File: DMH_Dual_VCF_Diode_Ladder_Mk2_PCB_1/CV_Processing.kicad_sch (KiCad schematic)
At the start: 46 parts, among them J15 Conn_01x08_PinHeader, J16 Conn_01x08_PinHeader, SW10 SW_DPDT_OnOn, SW7 SW_SPDT_OnOffOn, SW9 SW_SPDT_OnOffOn, U7 TL074, U8 TL074

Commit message: Corrected pin header footprint assignments
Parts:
- J15, J16: footprint Connector_PinHeader_2.54mm:PinHeader_1x10_P2.54mm_Vertical -> Connector_PinHeader_2.54mm:PinHeader_1x08_P2.54mm_Vertical
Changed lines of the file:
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@@
 			)
 		)
-		(property "Footprint" "Connector_PinHeader_2.54mm:PinHeader_1x10_P2.54mm_Vertical"
+		(property "Footprint" "Connector_PinHeader_2.54mm:PinHeader_1x08_P2.54mm_Vertical"
 			(at 69.85 106.68 0)
 			(effects
@@
 			)
 		)
-		(property "Footprint" "Connector_PinHeader_2.54mm:PinHeader_1x10_P2.54mm_Vertical"
+		(property "Footprint" "Connector_PinHeader_2.54mm:PinHeader_1x08_P2.54mm_Vertical"
 			(at 63.5 81.28 0)
 			(effects
@@
 			)
 		)
-		(property "Footprint" "Connector_PinHeader_2.54mm:PinHeader_1x10_P2.54mm_Vertical"
+		(property "Footprint" "Connector_PinHeader_2.54mm:PinHeader_1x08_P2.54mm_Vertical"
 			(at 119.38 38.1 0)
 			(effects
@@
 			)
 		)
-		(property "Footprint" "Connector_PinHeader_2.54mm:PinHeader_1x10_P2.54mm_Vertical"
+		(property "Footprint" "Connector_PinHeader_2.54mm:PinHeader_1x08_P2.54mm_Vertical"
 			(at 160.02 101.6 0)
 			(effects
@@
 			)
 		)
-		(property "Footprint" "Connector_PinHeader_2.54mm:PinHeader_1x10_P2.54mm_Vertical"
+		(property "Footprint" "Connector_PinHeader_2.54mm:PinHeader_1x08_P2.54mm_Vertical"
 			(at 140.97 101.6 0)
 			(effects
@@
 			)
 		)
-		(property "Footprint" "Connector_PinHeader_2.54mm:PinHeader_1x10_P2.54mm_Vertical"
+		(property "Footprint" "Connector_PinHeader_2.54mm:PinHeader_1x08_P2.54mm_Vertical"
 			(at 52.07 201.93 0)
 			(effects
@@
 			)
 		)
-		(property "Footprint" "Connector_PinHeader_2.54mm:PinHeader_1x10_P2.54mm_Vertical"
+		(property "Footprint" "Connector_PinHeader_2.54mm:PinHeader_1x08_P2.54mm_Vertical"
 			(at 127 170.18 0)
 			(effects
@@
 			)
 		)
-		(property "Footprint" "Connector_PinHeader_2.54mm:PinHeader_1x10_P2.54mm_Vertical"
+		(property "Footprint" "Connector_PinHeader_2.54mm:PinHeader_1x08_P2.54mm_Vertical"
 			(at 38.1 182.88 0)
 			(effects
@@
 			)
 		)
-		(property "Footprint" "Connector_PinHeader_2.54mm:PinHeader_1x10_P2.54mm_Vertical"
+		(property "Footprint" "Connector_PinHeader_2.54mm:PinHeader_1x08_P2.54mm_Vertical"
 			(at 77.47 227.33 0)
 			(effects
@@
 			)
 		)
-		(property "Footprint" "Connector_PinHeader_2.54mm:PinHeader_1x10_P2.54mm_Vertical"
+		(property "Footprint" "Connector_PinHeader_2.54mm:PinHeader_1x08_P2.54mm_Vertical"
 			(at 77.47 100.33 0)
 			(effects
@@
 			)
 		)
-		(property "Footprint" "Connector_PinHeader_2.54mm:PinHeader_1x10_P2.54mm_Vertical"
+		(property "Footprint" "Connector_PinHeader_2.54mm:PinHeader_1x08_P2.54mm_Vertical"
 			(at 63.5 208.28 0)
 			(effects
@@
 			)
 		)
-		(property "Footprint" "Connector_PinHeader_2.54mm:PinHeader_1x10_P2.54mm_Vertical"
+		(property "Footprint" "Connector_PinHeader_2.54mm:PinHeader_1x08_P2.54mm_Vertical"
 			(at 140.97 177.8 0)
 			(effects
@@
 			)
 		)
-		(property "Footprint" "Connector_PinHeader_2.54mm:PinHeader_1x10_P2.54mm_Vertical"
+		(property "Footprint" "Connector_PinHeader_2.54mm:PinHeader_1x08_P2.54mm_Vertical"
 			(at 171.45 134.62 0)
 			(effects
@@
 			)
 		)
-		(property "Footprint" "Connector_PinHeader_2.54mm:PinHeader_1x10_P2.54mm_Vertical"
+		(property "Footprint" "Connector_PinHeader_2.54mm:PinHeader_1x08_P2.54mm_Vertical"
 			(at 38.1 55.88 0)
 			(effects
@@
 			)
 		)
-		(property "Footprint" "Connector_PinHeader_2.54mm:PinHeader_1x10_P2.54mm_Vertical"
+		(property "Footprint" "Connector_PinHeader_2.54mm:PinHeader_1x08_P2.54mm_Vertical"
 			(at 52.07 74.93 0)
 			(effects
@@
 			)
 		)
-		(property "Footprint" "Connector_PinHeader_2.54mm:PinHeader_1x10_P2.54mm_Vertical"
+		(property "Footprint" "Connector_PinHeader_2.54mm:PinHeader_1x08_P2.54mm_Vertical"
 			(at 69.85 233.68 0)
 			(effects

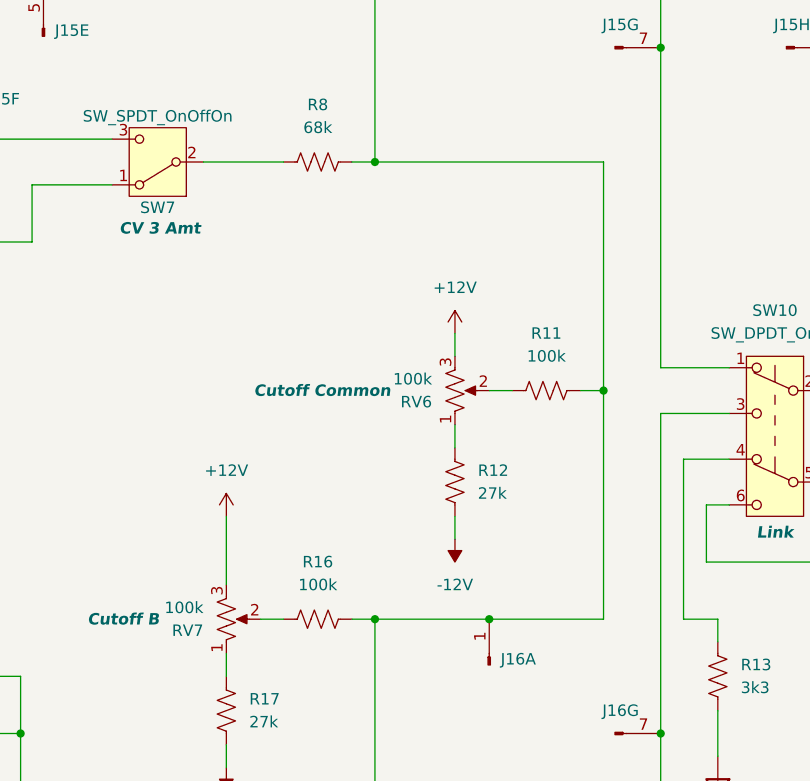
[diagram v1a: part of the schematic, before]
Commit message: Replaced Central Cutoff pot with dual port
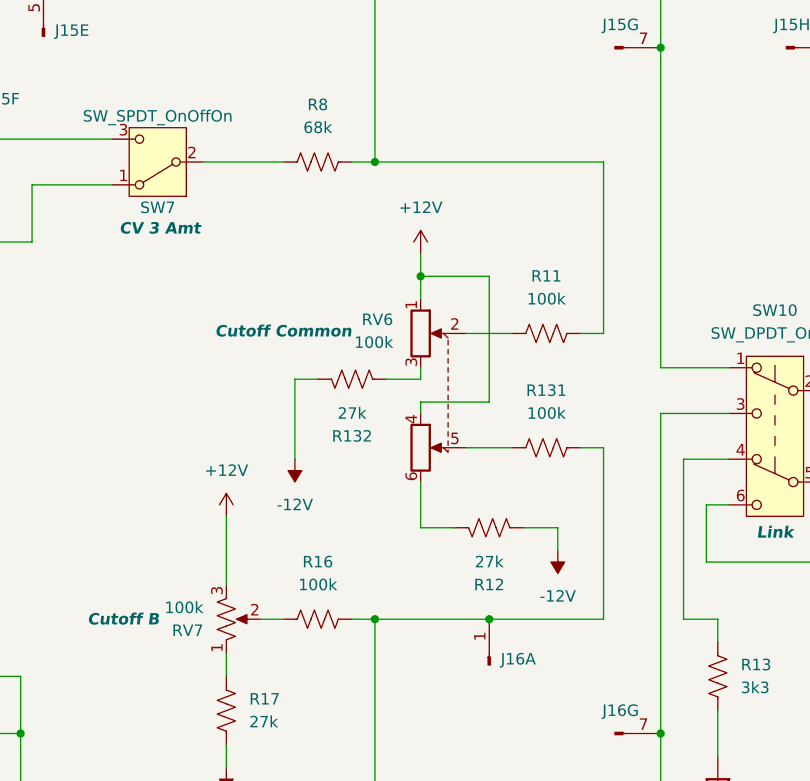
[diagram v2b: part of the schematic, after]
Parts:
- removed RV6: 100k, SynthStuff:Potentiometer_Alpha_RD901F-40-00D_Single_Vertical, symbol Device:R_Potentiometer_US
- added R131: 100k, Resistor_THT:R_Axial_DIN0207_L6.3mm_D2.5mm_P7.62mm_Horizontal, symbol Device:R_US
- added R132: 27k, Resistor_THT:R_Axial_DIN0207_L6.3mm_D2.5mm_P7.62mm_Horizontal, symbol Device:R_US
- added RV6: 100k, Potentiometer_THT:Potentiometer_Alpha_RD902F-40-00D_Dual_Vertical, symbol Device:R_Potentiometer_Dual
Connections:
- net +12V: now also RV6.1, RV6.4
- net -12V: now also R12.1, R132.2; no longer R12.2
- net at J15.1 (Pin_1), R1.2, R11.2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: no longer J16.1 (Pin_1), R16.2, R19.2, R20.1, R22.2, R23.1, U8.13 (-)
- net at R11.1: now also RV6.2
- new net: J16.1 (Pin_1), R131.2, R16.2, R19.2, R20.1, R22.2, R23.1, U8.13 (-)
- new net: R131.1, RV6.5
- new net: R12.2, RV6.6
- new net: R132.1, RV6.3
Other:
- moved on the sheet: R11, R12

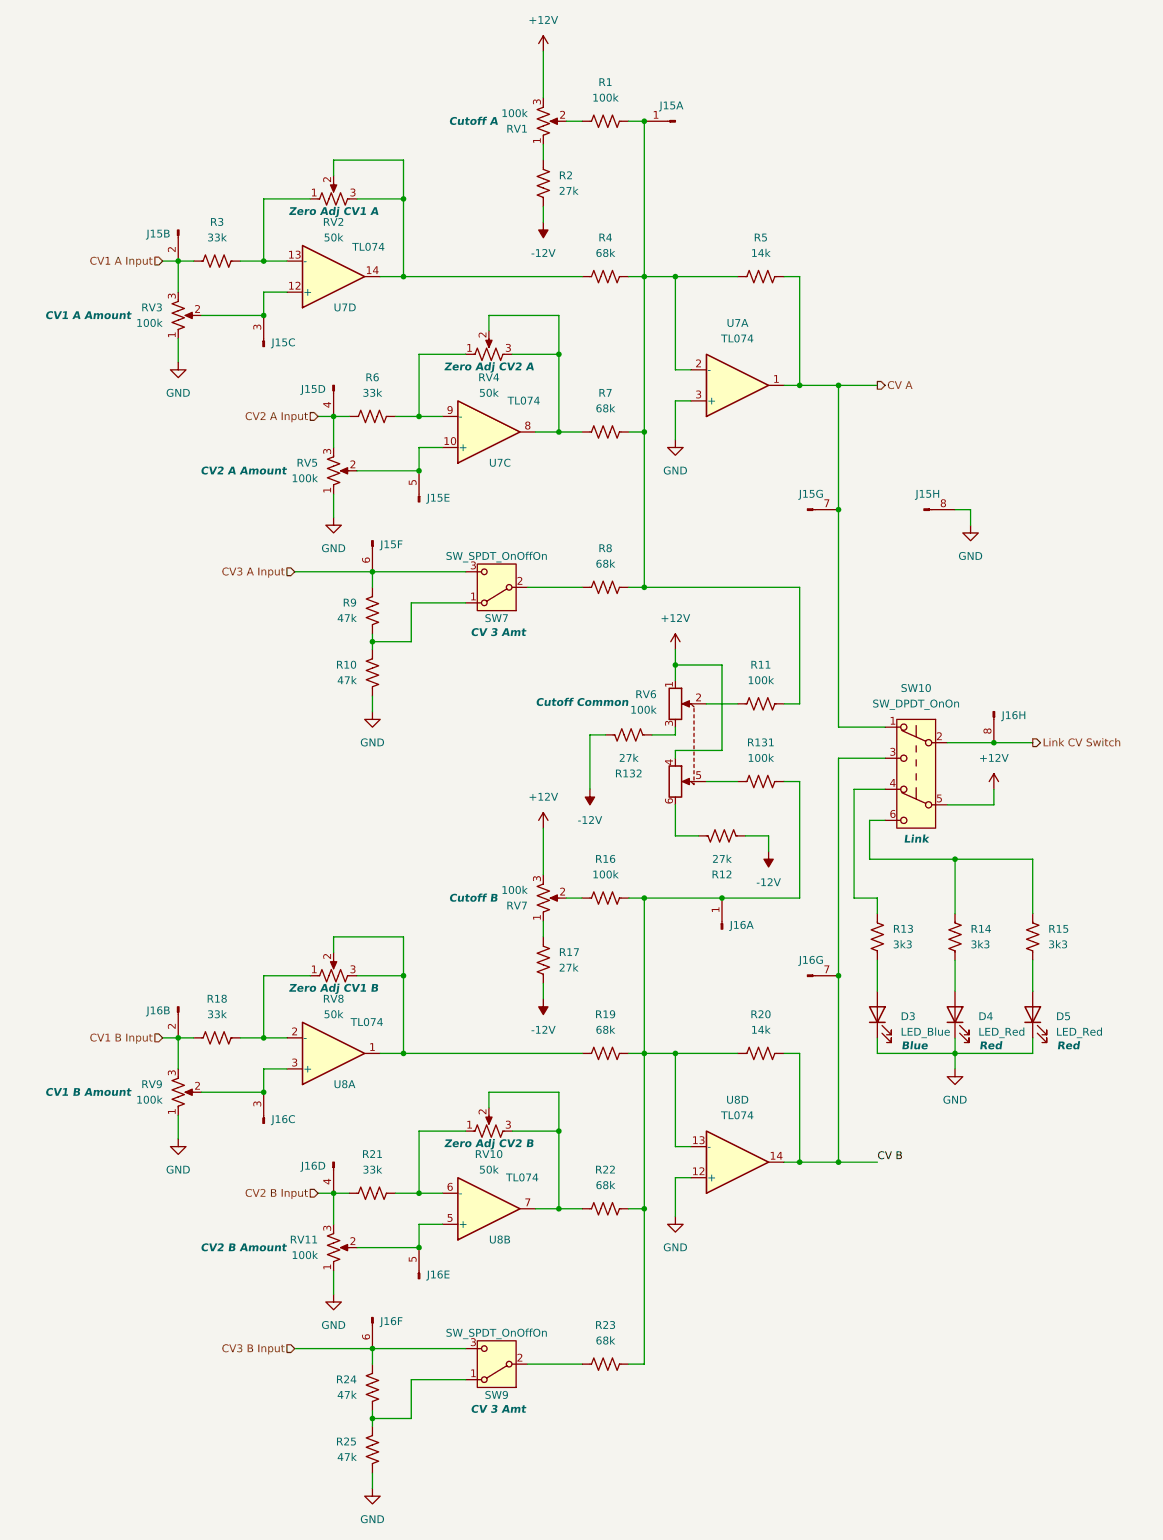
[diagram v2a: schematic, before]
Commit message: Routed circuit B
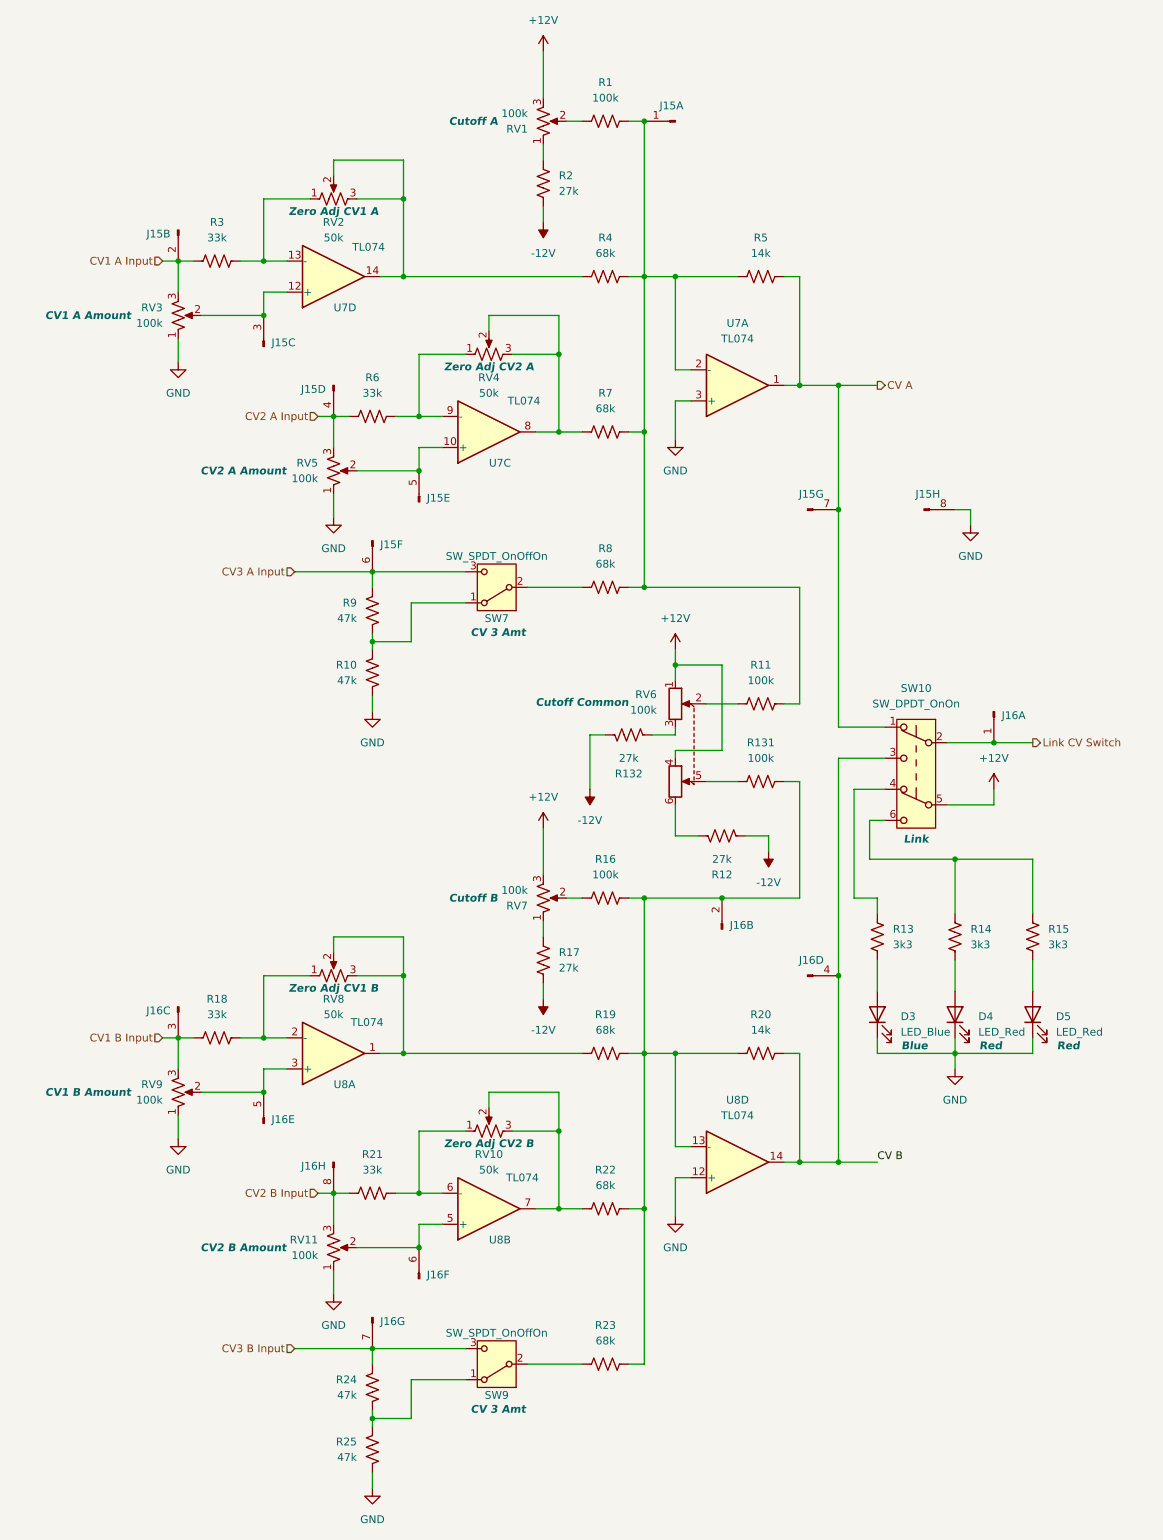
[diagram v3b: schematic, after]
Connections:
- net CV B: now also J16.4 (Pin_4); no longer J16.7 (Pin_7)
- net CV1 B Input: now also J16.3 (Pin_3); no longer J16.2 (Pin_2)
- net CV2 B Input: now also J16.8 (Pin_8); no longer J16.4 (Pin_4)
- net CV3 B Input: now also J16.7 (Pin_7); no longer J16.6 (Pin_6)
- net Link CV Switch: now also J16.1 (Pin_1); no longer J16.8 (Pin_8)
- net at R131.2, R16.2, R19.2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: now also J16.2 (Pin_2); no longer J16.1 (Pin_1)
- net at RV11.2, U8.5 (+): now also J16.6 (Pin_6); no longer J16.5 (Pin_5)
- net at RV9.2, U8.3 (+): now also J16.5 (Pin_5); no longer J16.3 (Pin_3)
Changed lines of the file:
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@@
 		(at 52.07 201.93 270)
 		(mirror x)
-		(unit 3)
+		(unit 5)
 		(exclude_from_sim no)
 		(in_bom yes)
@@
 				(path "/58f4306d-5387-4983-bb08-41a2313fd315/ec2d44bc-ed06-4f0b-a22e-df640fa5e089"
 					(reference "J16")
-					(unit 3)
+					(unit 5)
 				)
 			)
@@
 		(lib_id "SynthStuff:Conn_01x08_PinHeader")
 		(at 127 170.18 90)
-		(unit 1)
+		(unit 2)
 		(exclude_from_sim no)
 		(in_bom yes)
@@
 				(path "/58f4306d-5387-4983-bb08-41a2313fd315/ec2d44bc-ed06-4f0b-a22e-df640fa5e089"
 					(reference "J16")
-					(unit 1)
+					(unit 2)
 				)
 			)
@@
 		(at 38.1 182.88 90)
 		(mirror x)
-		(unit 2)
+		(unit 3)
 		(exclude_from_sim no)
 		(in_bom yes)
@@
 				(path "/58f4306d-5387-4983-bb08-41a2313fd315/ec2d44bc-ed06-4f0b-a22e-df640fa5e089"
 					(reference "J16")
-					(unit 2)
+					(unit 3)
 				)
 			)
@@
 		(lib_id "SynthStuff:Conn_01x08_PinHeader")
 		(at 77.47 227.33 90)
-		(unit 5)
+		(unit 6)
 		(exclude_from_sim no)
 		(in_bom yes)
@@
 				(path "/58f4306d-5387-4983-bb08-41a2313fd315/ec2d44bc-ed06-4f0b-a22e-df640fa5e089"
 					(reference "J16")
-					(unit 5)
+					(unit 6)
 				)
 			)
@@
 		(at 63.5 208.28 90)
 		(mirror x)
-		(unit 4)
+		(unit 8)
 		(exclude_from_sim no)
 		(in_bom yes)
@@
 				(path "/58f4306d-5387-4983-bb08-41a2313fd315/ec2d44bc-ed06-4f0b-a22e-df640fa5e089"
 					(reference "J16")
-					(unit 4)
+					(unit 8)
 				)
 			)
@@
 		(lib_id "SynthStuff:Conn_01x08_PinHeader")
 		(at 140.97 177.8 0)
-		(unit 7)
+		(unit 4)
 		(exclude_from_sim no)
 		(in_bom yes)
@@
 				(path "/58f4306d-5387-4983-bb08-41a2313fd315/ec2d44bc-ed06-4f0b-a22e-df640fa5e089"
 					(reference "J16")
-					(unit 7)
+					(unit 4)
 				)
 			)
@@
 		(lib_id "SynthStuff:Conn_01x08_PinHeader")
 		(at 171.45 134.62 270)
-		(unit 8)
+		(unit 1)
 		(exclude_from_sim no)
 		(in_bom yes)
@@
 				(path "/58f4306d-5387-4983-bb08-41a2313fd315/ec2d44bc-ed06-4f0b-a22e-df640fa5e089"
 					(reference "J16")
-					(unit 8)
+					(unit 1)
 				)
 			)
@@
 		(lib_id "SynthStuff:Conn_01x08_PinHeader")
 		(at 69.85 233.68 270)
-		(unit 6)
+		(unit 7)
 		(exclude_from_sim no)
 		(in_bom yes)
@@
 				(path "/58f4306d-5387-4983-bb08-41a2313fd315/ec2d44bc-ed06-4f0b-a22e-df640fa5e089"
 					(reference "J16")
-					(unit 6)
+					(unit 7)
 				)
 			)
